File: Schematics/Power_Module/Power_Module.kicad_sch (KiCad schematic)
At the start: 43 parts, among them J1 ScrewSwitch A, J2 ScrewSwitch B, J3 Battery B, J5 Battery A, J6 Stack Male Edge Connector, Q1 AO4485, Q2 AO4485, U1 LMR51430XDDCR, U2 LMR51430XDDCR, U3 LMR51430XDDCR

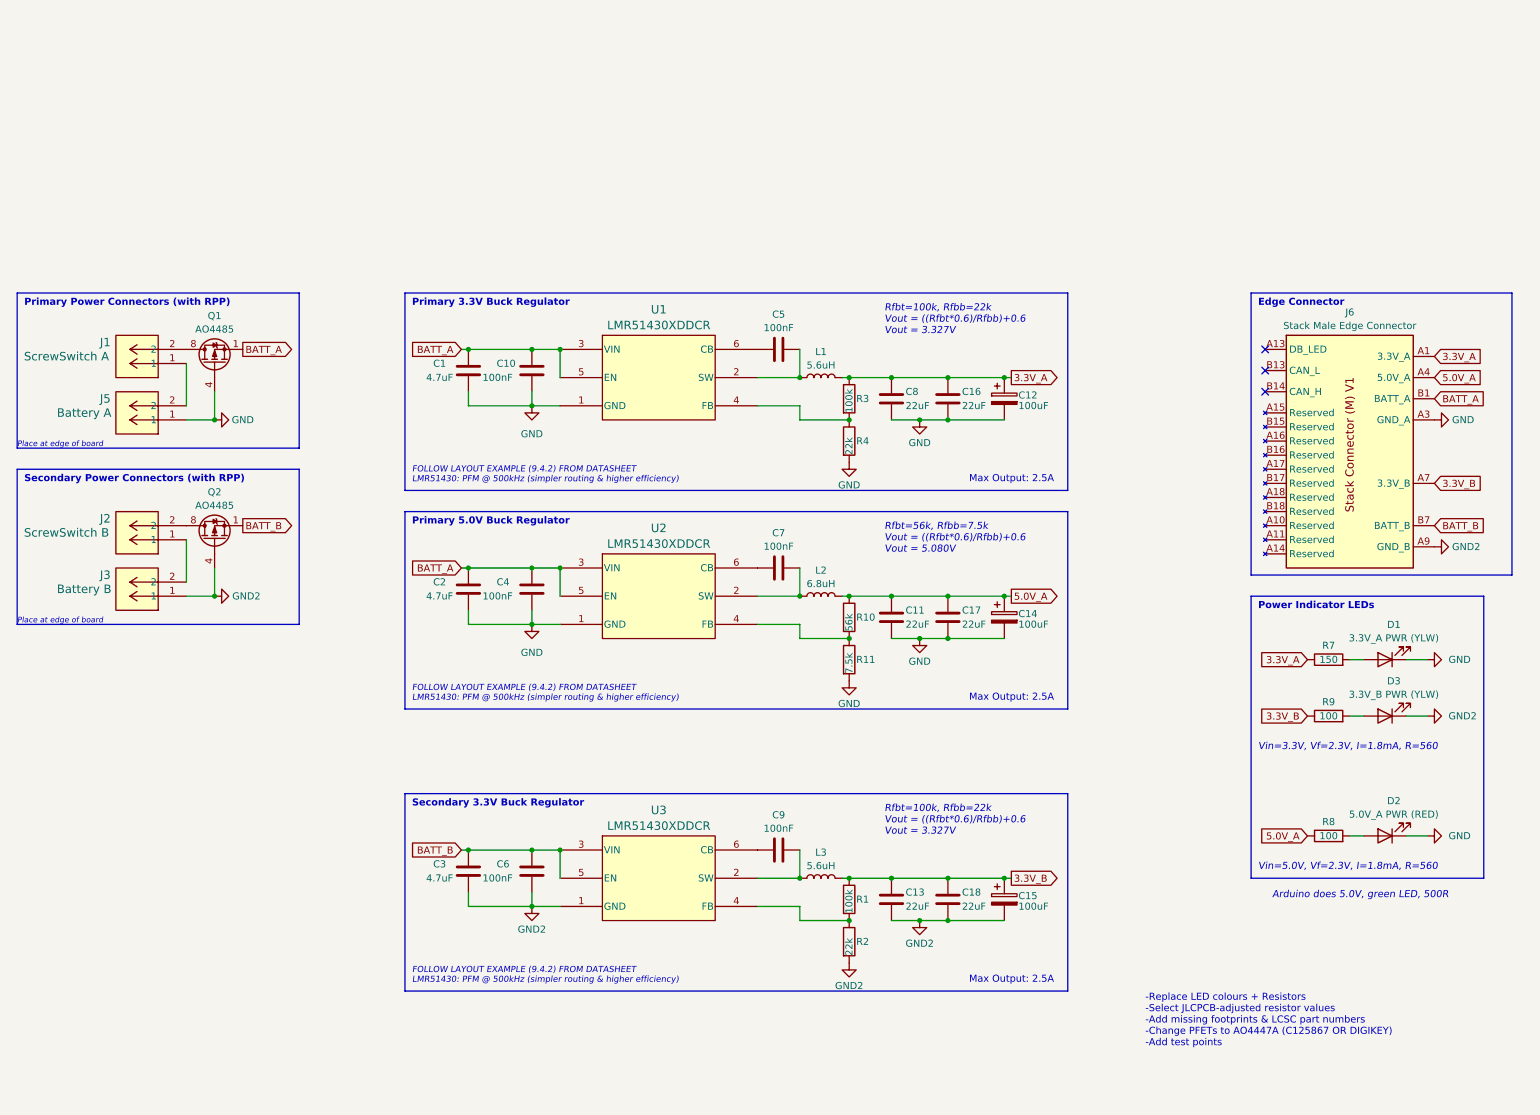
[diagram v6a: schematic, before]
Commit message: Small tweaks
-Added testpoints
-Upgrade reverse polarity protection from AO4485 to to AO4447A
-Selected LED colours & resistors
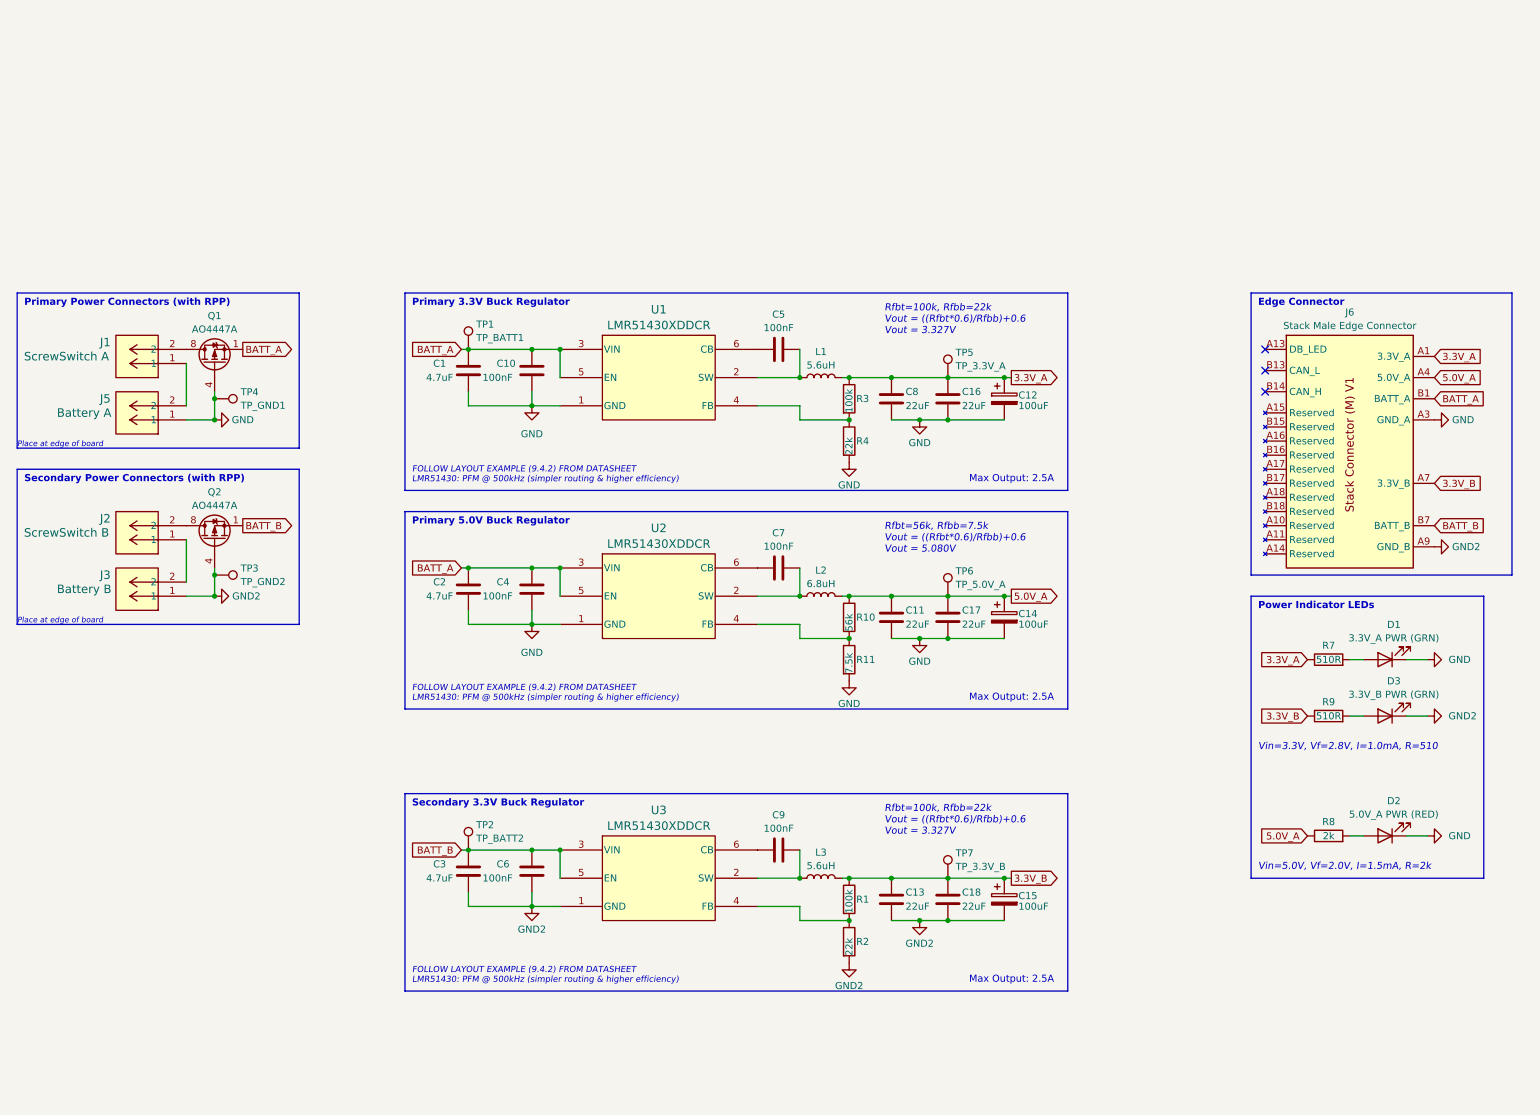
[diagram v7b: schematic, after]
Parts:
- added TP1: TP_BATT1, TestPoint:TestPoint_Pad_2.0x2.0mm, symbol Connector:TestPoint
- added TP2: TP_BATT2, TestPoint:TestPoint_Pad_2.0x2.0mm, symbol Connector:TestPoint
- added TP3: TP_GND2, TestPoint:TestPoint_Pad_2.0x2.0mm, symbol Connector:TestPoint
- added TP4: TP_GND1, TestPoint:TestPoint_Pad_2.0x2.0mm, symbol Connector:TestPoint
- added TP5: TP_3.3V_A, TestPoint:TestPoint_Pad_2.0x2.0mm, symbol Connector:TestPoint
- added TP6: TP_5.0V_A, TestPoint:TestPoint_Pad_2.0x2.0mm, symbol Connector:TestPoint
- added TP7: TP_3.3V_B, TestPoint:TestPoint_Pad_2.0x2.0mm, symbol Connector:TestPoint
- D1: value 3.3V_A PWR (YLW) -> 3.3V_A PWR (GRN); footprint LED_SMD:LED_0603_1608Metric -> LED_SMD:LED_0805_2012Metric; LCSC C2290 -> C2297
- D2: footprint LED_SMD:LED_0603_1608Metric -> LED_SMD:LED_0805_2012Metric; LCSC C2286 -> C84256
- D3: value 3.3V_B PWR (YLW) -> 3.3V_B PWR (GRN); footprint LED_SMD:LED_0603_1608Metric -> LED_SMD:LED_0805_2012Metric; LCSC C2290 -> C2297
- Q1, Q2: value AO4485 -> AO4447A; LCSC C51499 -> C125867
- R7: value 150 -> 510R; LCSC (none) -> C23193
- R8: value 100 -> 2k; LCSC (none) -> C22975
- R9: value 100 -> 510R; LCSC (none) -> C23193
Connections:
- net 3.3V_A: now also TP5.1
- net 3.3V_B: now also TP7.1
- net 5.0V_A: now also TP6.1
- net BATT_A: now also TP1.1
- net BATT_B: now also TP2.1
- net GND: now also TP4.1
- net GND2: now also TP3.1
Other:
- note added: "Vin=3.3V, Vf=2.8V, I=1.0mA, R=510"
- note added: "Vin=5.0V, Vf=2.0V, I=1.5mA, R=2k"
- note removed: "-Replace LED colours + Resistors -Select JLCPCB-adjusted resistor values -Add missing footprints & LCSC part numbers -Change PFETs to AO4447A (C125867 OR DIGIKEY) -Add test points"
- note removed: "Arduino does 5.0V, green LED, 500R"
- note removed: "Vin=3.3V, Vf=2.3V, I=1.8mA, R=560"
- note removed: "Vin=5.0V, Vf=2.3V, I=1.8mA, R=560"

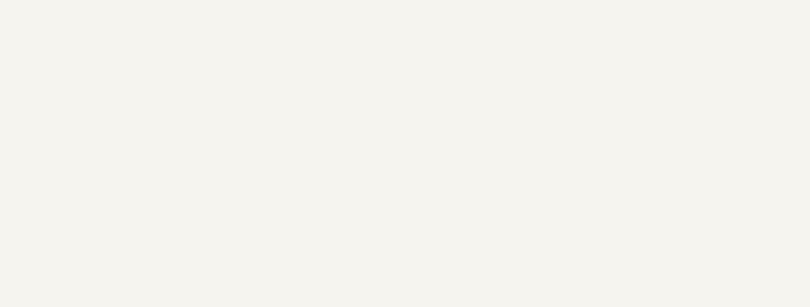
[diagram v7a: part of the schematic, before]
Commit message: Layout of 3.3V_A converter finished
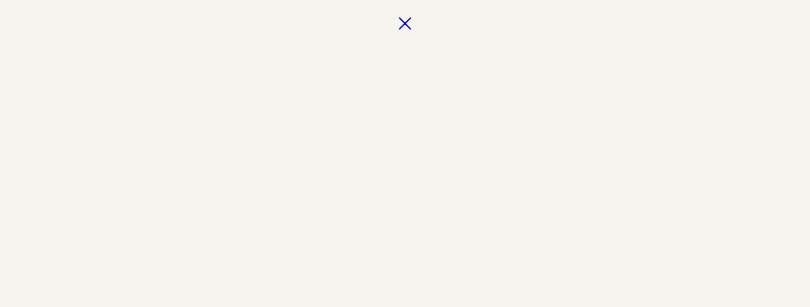
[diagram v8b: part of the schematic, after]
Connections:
- no-connect marks 3 -> 4
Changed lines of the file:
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@@
   (no_connect (at 238.76 27.94))
   (no_connect (at 238.76 31.75))
+  (no_connect (at 73.66 -36.195))
   (wire (pts (xy 49.53 31.75) (xy 49.53 33.02))
     (stroke (width 0) (type default))
